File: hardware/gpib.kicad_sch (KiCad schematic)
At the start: 24 parts, among them J1 112-024-113R001, U3 SN75160BDW, U4 SN75161BDW

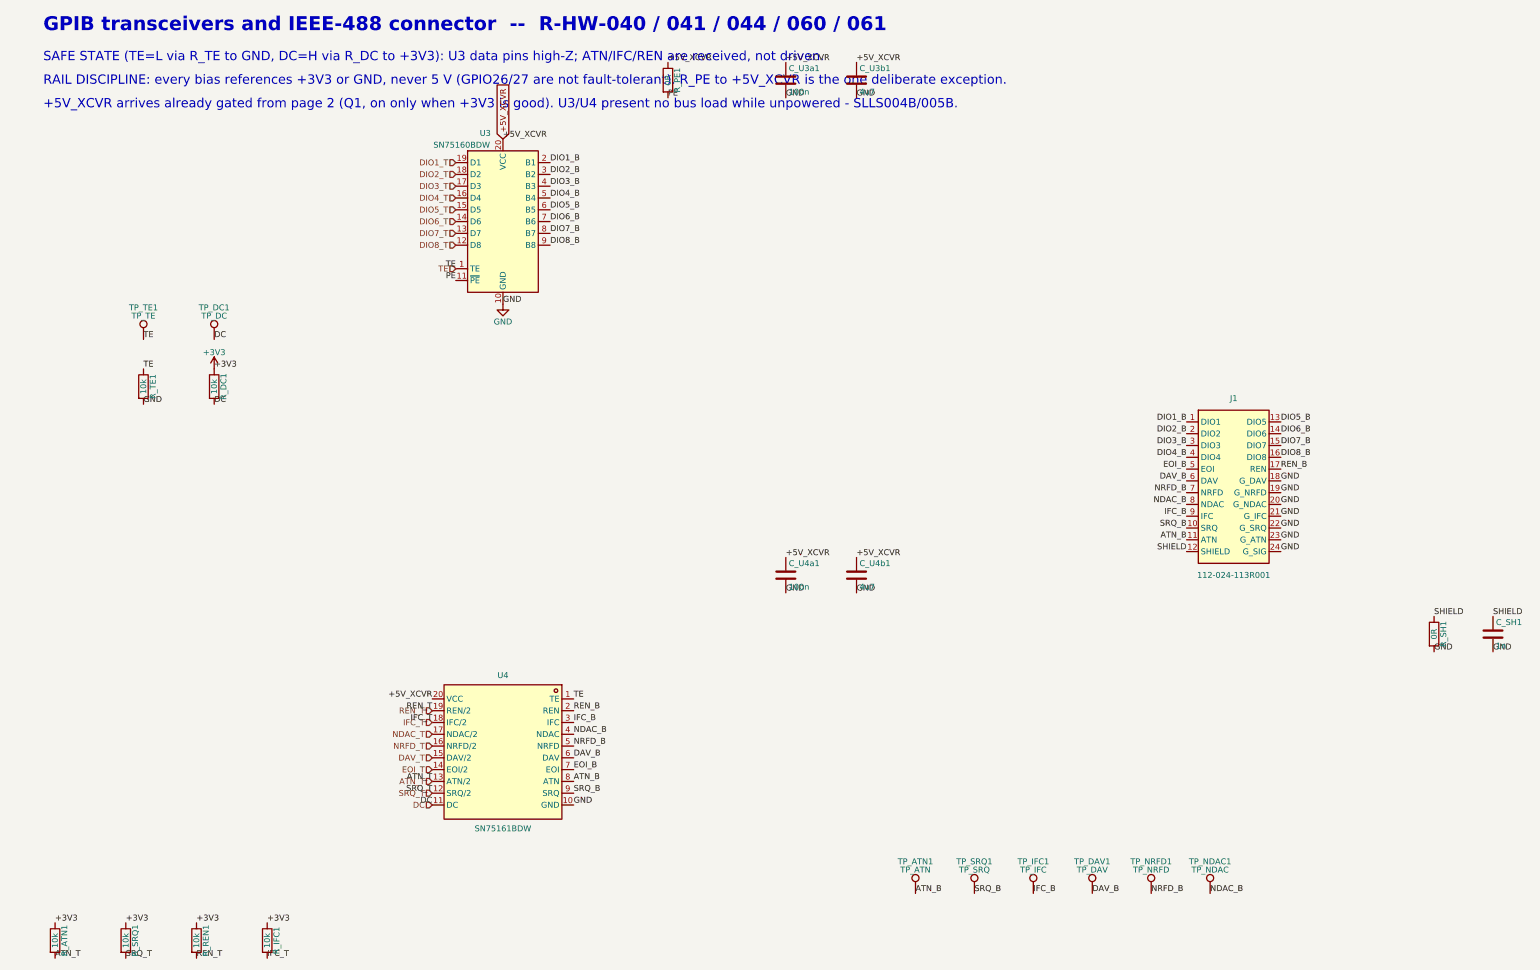
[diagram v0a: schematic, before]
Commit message: hardware: updated board design (reference renumbering, LED polarity fix, crystal symbol upgrade)
Replaces the schematics/PCB/project file with the latest design. Key
changes, verified before committing (netlist-check.py: 124 checks, 0
failures; ERC unchanged at 3 known pin_not_driven findings on W5500 SPI
inputs, same severity-policy artifact as before):

- Component reference designators changed from descriptive names
  (R_ATN, C_3V3, D_BR1, etc.) to plain auto-numbered ones (R15, C9, D1,
  etc.) -- intentional, since descriptive names were ending up on the
  silkscreen; they belong in the BOM instead. docs/netlist-spec.nets
  updated to match via a UUID-verified old-ref -> new-ref mapping (every
  renamed symbol's KiCad UUID was unchanged, confirming these are pure
  renames with no electrical difference), not a hand transcription.
- LED1's wiring was corrected: the old schematic had its anode tied to
  GND and cathode driven by LED_A (backwards -- confirmed via each net's
  pinfunction annotation in the exported netlist, K_1/A_2, which is
  fixed by the Device:LED symbol regardless of reference numbering).
  The new schematic has cathode-to-GND, anode-to-LED_A, the correct
  orientation.
- X1/X2 changed from Device:Crystal (2-pin) to Device:Crystal_GND24
  (4-pin, case-ground on pins 2/4) -- a more accurate symbol for the
  real SMD crystal package. netlist-spec.nets updated accordingly
  (XOUT/ETH_XO now reference pin 3, GND gained the four case pins).

mcu.kicad_sch was supplied separately (missing from the first archive);
confirmed it has no further sub-sheet references and all its symbols'
footprint names resolve against the existing hardware/lib/adapter.pretty/
library, which was deliberately left untouched along with fp-lib-table,
sym-lib-table, and .konnect/ -- none of those changed in this update.
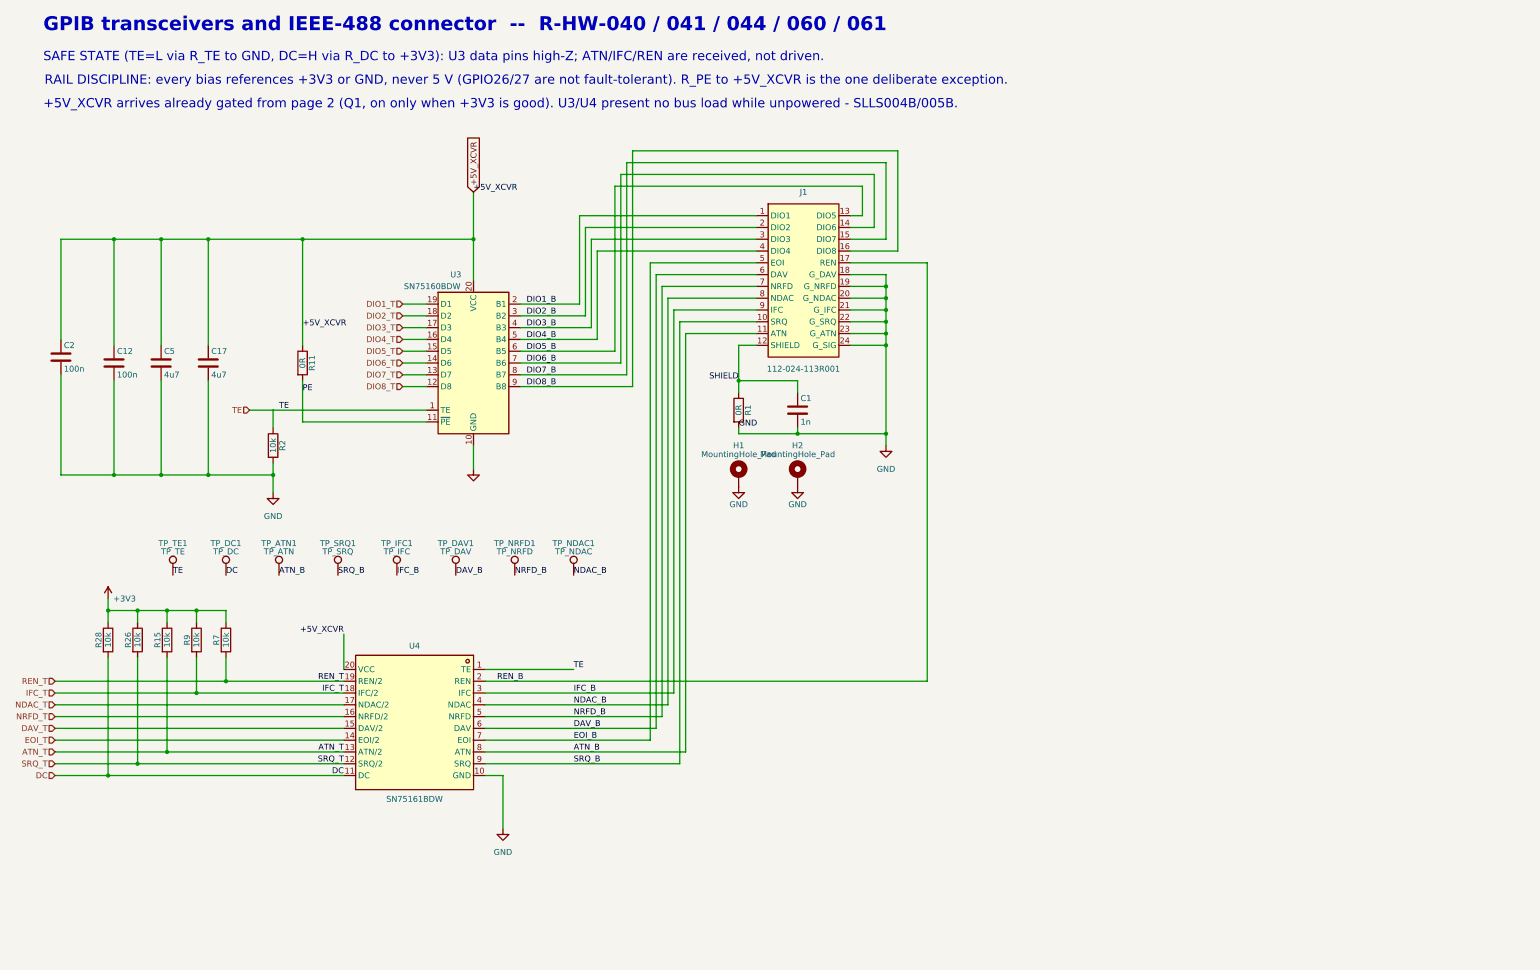
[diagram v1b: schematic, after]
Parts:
- added H1, H2: MountingHole_Pad, MountingHole:MountingHole_3.2mm_M3_Pad, symbol Mechanical:MountingHole_Pad
- C12: renamed from C_U3a1; LCSC (none) -> C49678
- C17: renamed from C_U3b1; LCSC (none) -> C1779
- C2: renamed from C_U4a1; LCSC (none) -> C49678
- C5: renamed from C_U4b1; LCSC (none) -> C1779
- R2: renamed from R_TE1; LCSC (none) -> C17414
- U4: LCSC (none) -> C139410
- renumbered C_SH1 to C1, R_SH1 to R1, R_PE1 to R11, R_ATN1 to R15, R_SRQ1 to R26, R_DC1 to R28, R_REN1 to R7, R_IFC1 to R9
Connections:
- net GND: now also H1.1, H2.1
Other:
- moved on the sheet: C1, C12, C17, C2, C5, J1, R1, R11, R15, R2, R26, R28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
